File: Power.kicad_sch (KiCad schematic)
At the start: 4 parts, among them U1 L7805

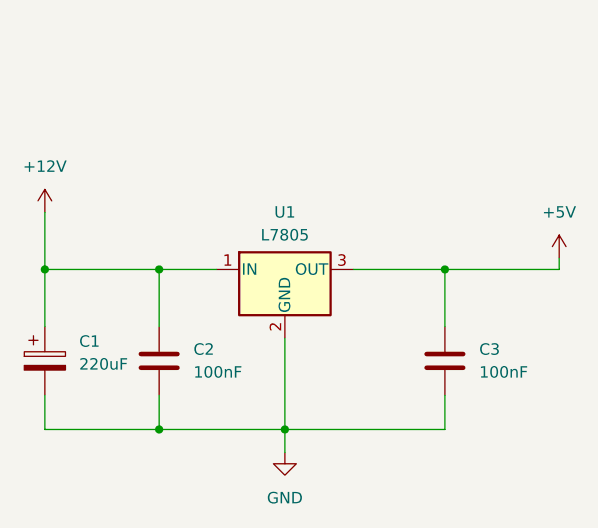
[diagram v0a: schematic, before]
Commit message: Correction in designators.
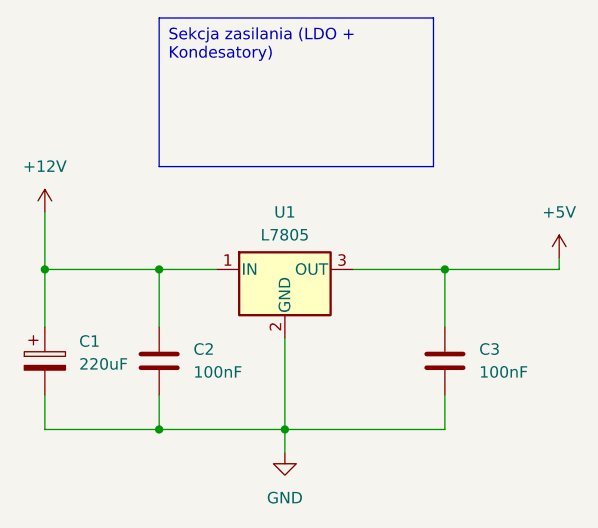
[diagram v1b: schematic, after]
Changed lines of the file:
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@@
+		)
+	)
+	(text_box "Sekcja zasilania (LDO + Kondesatory)"
+		(exclude_from_sim no)
+		(at 119.38 39.37 0)
+		(size 30.48 16.51)
+		(stroke
+			(width 0)
+			(type default)
+		)
+		(fill
+			(type none)
+		)
+		(effects
+			(font
+				(size 1.27 1.27)
+			)
+			(justify left top)
 		)
 	)
